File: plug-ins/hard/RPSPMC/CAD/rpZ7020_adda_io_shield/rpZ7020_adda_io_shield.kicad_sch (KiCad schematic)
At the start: 24 parts, among them J1 Samtec_ASP-134486-01, J2-FMC-RP1 Conn_02x20, J3-FMC-POWER1 Conn_02x06_Odd_Even, J4-FMC-AUX1 Conn_02x06_Odd_Even

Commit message: finialy Rev1.0.0, in production.
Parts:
- added J2: Conn_01x03_Socket, Connector_PinSocket_2.54mm:PinSocket_1x03_P2.54mm_Vertical, symbol Connector:Conn_01x03_Socket
- C1, C2, C3, C4, C5, C6: footprint Capacitor_THT:C_Rect_L4.6mm_W2.0mm_P2.50mm_MKS02_FKP02 -> Capacitor_SMD:C_1206_3216Metric_Pad1.33x1.80mm_HandSolder
- J2-FMC-RP1: now not fitted
- renumbered JPMD1 to PMD1, JPMD2 to PMD2, JPMD3 to PMD3, JPMD4 to PMD4, JPMD5 to PMD5, JPMD6 to PMD6, TP-CLK1 to TP-CLK, TP-SYNC1 to TP-SYNC
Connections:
- net EXT 3.3V DAC: now also J2.2 (Pin_2)
- net GND: now also J2.1 (Pin_1)
- new net 5V USB: J2.3 (Pin_3)
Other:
- note added: "USB 5V 3.3V Regulator Module Option"

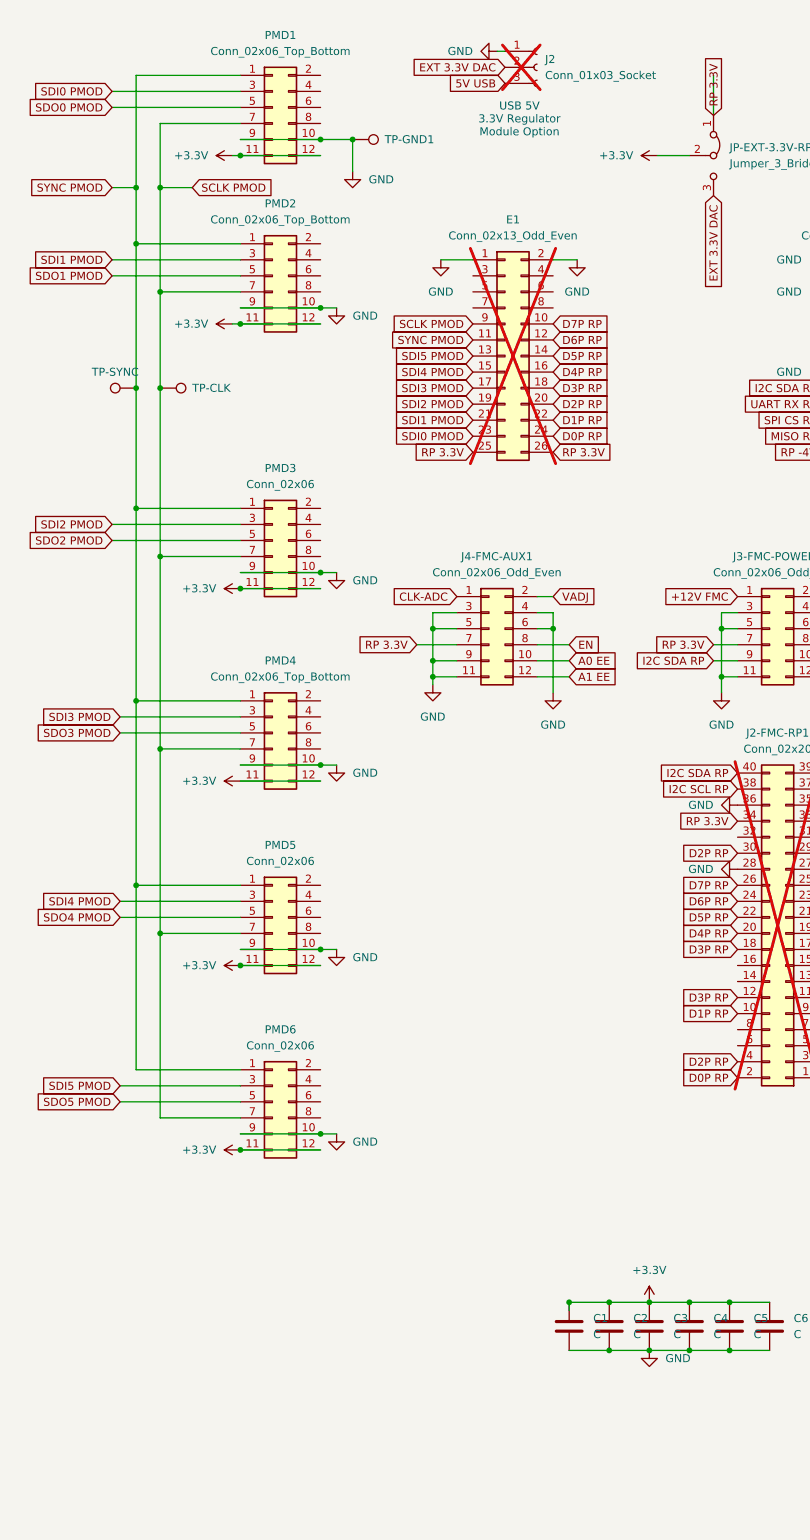
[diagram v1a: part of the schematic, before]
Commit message: patch to PCB, PMOD connector mirror issue, but no issue, easy fix. completed AD463x SPI IP -- to be tested and integarted into signals, added selector added Z-polarity switch
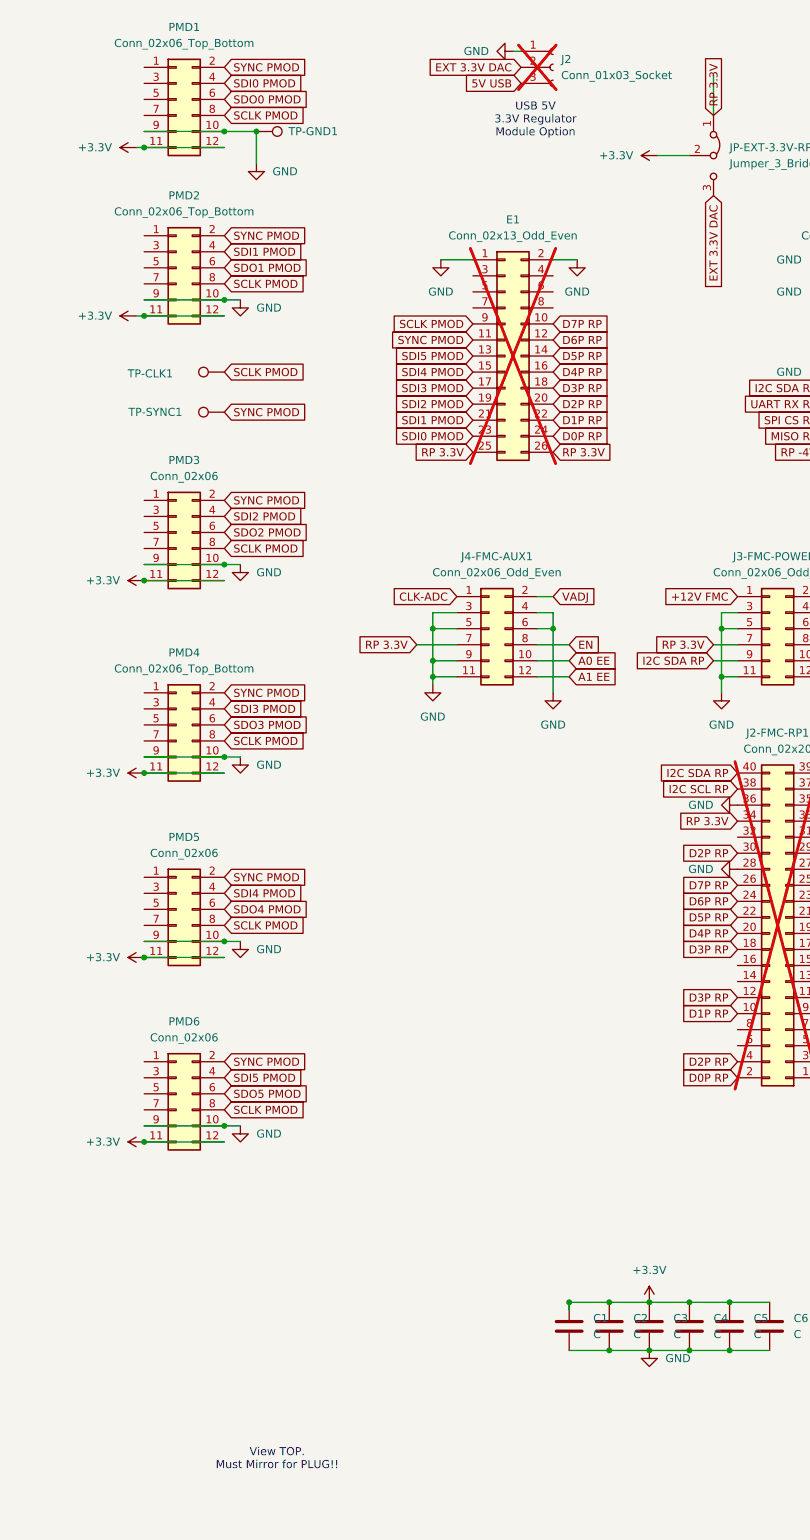
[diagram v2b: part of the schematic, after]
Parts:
- renumbered TP-CLK to TP-CLK1, TP-SYNC to TP-SYNC1
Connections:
- net SCLK PMOD: now also PMD1.8 (Pin_8), PMD2.8 (Pin_8), PMD3.8 (Pin_8), PMD4.8 (Pin_8), PMD5.8 (Pin_8), PMD6.8 (Pin_8); no longer PMD1.7 (Pin_7), PMD2.7 (Pin_7), PMD3.7 (Pin_7), PMD4.7 (Pin_7), PMD5.7 (Pin_7), PMD6.7 (Pin_7)
- net SDI0 PMOD: now also PMD1.4 (Pin_4); no longer PMD1.3 (Pin_3)
- net SDI1 PMOD: now also PMD2.4 (Pin_4); no longer PMD2.3 (Pin_3)
- net SDI2 PMOD: now also PMD3.4 (Pin_4); no longer PMD3.3 (Pin_3)
- net SDI3 PMOD: now also PMD4.4 (Pin_4); no longer PMD4.3 (Pin_3)
- net SDI4 PMOD: now also PMD5.4 (Pin_4); no longer PMD5.3 (Pin_3)
- net SDI5 PMOD: now also PMD6.4 (Pin_4); no longer PMD6.3 (Pin_3)
- net SDO0 PMOD: now also PMD1.6 (Pin_6); no longer PMD1.5 (Pin_5)
- net SDO1 PMOD: now also PMD2.6 (Pin_6); no longer PMD2.5 (Pin_5)
- net SDO2 PMOD: now also PMD3.6 (Pin_6); no longer PMD3.5 (Pin_5)
- net SDO3 PMOD: now also PMD4.6 (Pin_6); no longer PMD4.5 (Pin_5)
- net SDO4 PMOD: now also PMD5.6 (Pin_6); no longer PMD5.5 (Pin_5)
- net SDO5 PMOD: now also PMD6.6 (Pin_6); no longer PMD6.5 (Pin_5)
- net SYNC PMOD: now also PMD1.2 (Pin_2), PMD2.2 (Pin_2), PMD3.2 (Pin_2), PMD4.2 (Pin_2), PMD5.2 (Pin_2), PMD6.2 (Pin_2); no longer PMD1.1 (Pin_1), PMD2.1 (Pin_1), PMD3.1 (Pin_1), PMD4.1 (Pin_1), PMD5.1 (Pin_1), PMD6.1 (Pin_1)
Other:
- note added: "View TOP. Must Mirror for PLUG!!"
- moved on the sheet: J2, PMD1, PMD2, PMD3, PMD4, PMD5, PMD6, TP-CLK1, TP-GND1, TP-SYNC1
